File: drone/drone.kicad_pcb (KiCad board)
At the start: 2 copper layers, 53.3 x 55.2 mm, 52 parts, among them U1 ESP32-WROOM-32D, U2 MPU-6050, U3 MP2303ADN

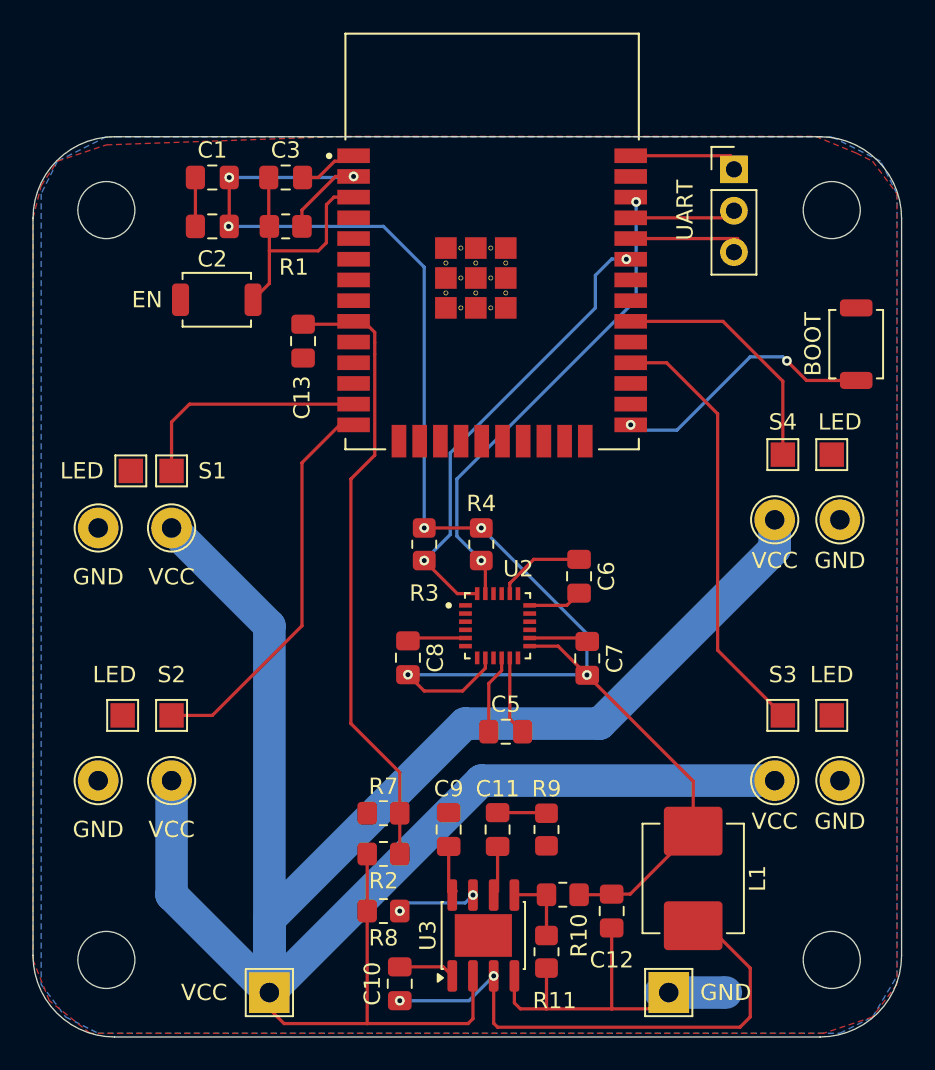
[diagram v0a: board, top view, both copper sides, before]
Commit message: tang width 3v3 len 0.4mm
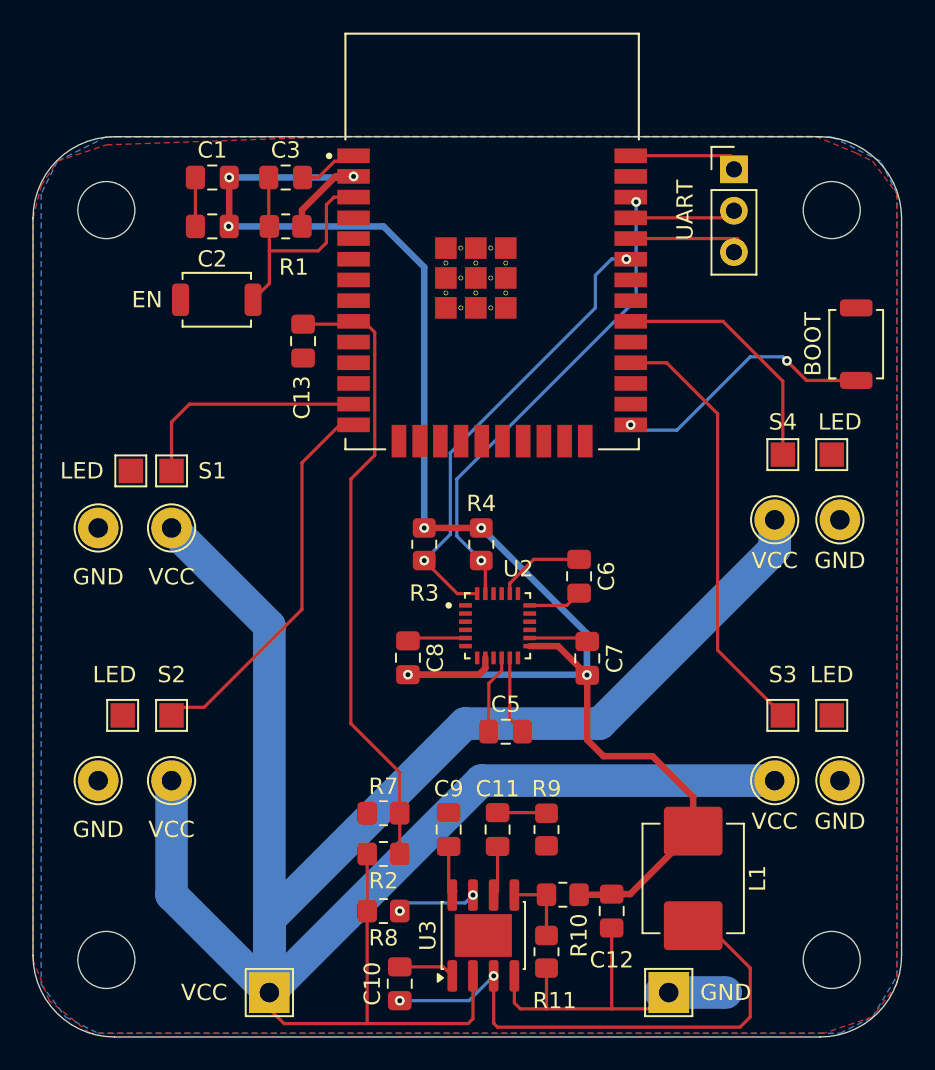
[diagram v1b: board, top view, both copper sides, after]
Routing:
- net +3V3: track 103.0 -> 103.9 mm
- net ESC2: track 24.4 -> 23.8 mm
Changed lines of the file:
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@@
 		(capping no)
 		(filling no)
+		(zone_defaults)
 		(pcbplotparams
 			(layerselection 0x00000000_00000000_55555555_5755f5ff)
@@
 	)
 	(segment
-		(start 203.5 74.5)
-		(end 205.565 72.435)
-		(width 0.2)
+		(start 219.2125 101.25)
+		(end 217.47 101.25)
+		(width 0.4)
 		(layer "F.Cu")
 		(net "+3V3")
 	)
 	(segment
-		(start 219.2125 101.25)
-		(end 220.98125 103.01875)
-		(width 0.2)
+		(start 210 103)
+		(end 214.355 103)
+		(width 0.4)
 		(layer "F.Cu")
 		(net "+3V3")
 	)
 	(segment
-		(start 203.5 75.5)
-		(end 203.5 74.5)
-		(width 0.2)
+		(start 225 108)
+		(end 222 108)
+		(width 0.4)
 		(layer "F.Cu")
 		(net "+3V3")
 	)
 	(segment
-		(start 227.5 109.5375)
-		(end 227.5 112.6)
-		(width 0.2)
+		(start 227.5 110.5)
+		(end 225 108)
+		(width 0.4)
 		(layer "F.Cu")
 		(net "+3V3")
 	)
 	(segment
-		(start 199.0375 72.5)
-		(end 199.0375 76)
-		(width 0.2)
+		(start 203.5 74.5)
+		(end 205.565 72.435)
+		(width 0.4)
 		(layer "F.Cu")
 		(net "+3V3")
 	)
 	(segment
-		(start 213.355 104)
-		(end 211 104)
-		(width 0.2)
+		(start 214.355 103)
+		(end 214.75 102.605)
+		(width 0.4)
 		(layer "F.Cu")
 		(net "+3V3")
 	)
 	(segment
-		(start 214.75 102.605)
-		(end 213.355 104)
-		(width 0.2)
+		(start 203.5 75.5)
+		(end 203.5 74.5)
+		(width 0.4)
 		(layer "F.Cu")
 		(net "+3V3")
 	)
 	(segment
-		(start 220.98125 103.01875)
-		(end 221 103.0375)
-		(width 0.2)
+		(start 199.0375 72.5)
+		(end 199.0375 76)
+		(width 0.4)
 		(layer "F.Cu")
 		(net "+3V3")
 	)
 	(segment
-		(start 205.565 72.435)
-		(end 206.665 72.435)
-		(width 0.2)
+		(start 214.75 102.605)
+		(end 214.75 101.97)
+		(width 0.4)
 		(layer "F.Cu")
 		(net "+3V3")
 	)
 	(segment
-		(start 214.75 101.97)
-		(end 214.75 102.605)
-		(width 0.2)
+		(start 223.6375 116.4625)
+		(end 227.5 112.6)
+		(width 0.4)
 		(layer "F.Cu")
 		(net "+3V3")
 	)
 	(segment
-		(start 222.5 116.4625)
+		(start 220.5 116.5)
 		(end 222.4625 116.5)
-		(width 0.2)
+		(width 0.4)
 		(layer "F.Cu")
 		(net "+3V3")
 	)
 	(segment
-		(start 227.5 109.5375)
+		(start 221 107)
 		(end 221 103.0375)
-		(width 0.2)
+		(width 0.4)
 		(layer "F.Cu")
 		(net "+3V3")
 	)
 	(segment
-		(start 223.6375 116.4625)
-		(end 227.5 112.6)
-		(width 0.2)
+		(start 220.98125 103.01875)
+		(end 221 103.0375)
+		(width 0.4)
+		(layer "F.Cu")
+		(net "+3V3")
+	)
+	(segment
+		(start 205.565 72.435)
+		(end 206.665 72.435)
+		(width 0.4)
 		(layer "F.Cu")
 		(net "+3V3")
@@
 	(segment
 		(start 222.4625 116.5)
-		(end 220.5 116.5)
-		(width 0.2)
+		(end 222.5 116.4625)
+		(width 0.4)
+		(layer "F.Cu")
+		(net "+3V3")
+	)
+	(segment
+		(start 222 108)
+		(end 221 107)
+		(width 0.4)
 		(layer "F.Cu")
 		(net "+3V3")
 	)
 	(segment
-		(start 217.47 101.25)
+		(start 220.98125 103.01875)
 		(end 219.2125 101.25)
-		(width 0.2)
+		(width 0.4)
 		(layer "F.Cu")
 		(net "+3V3")
@@
 		(start 211 94)
 		(end 214.5 94)
-		(width 0.2)
+		(width 0.4)
 		(layer "F.Cu")
 		(net "+3V3")
@@
 		(start 222.5 116.4625)
 		(end 223.6375 116.4625)
-		(width 0.2)
+		(width 0.4)
 		(layer "F.Cu")
 		(net "+3V3")
 	)
 	(segment
-		(start 211 104)
-		(end 210 103)
-		(width 0.2)
+		(start 227.5 112.6)
+		(end 227.5 110.5)
+		(width 0.4)
 		(layer "F.Cu")
 		(net "+3V3")
@@
 		(start 199 75.5)
 		(end 199.0375 75.5)
-		(width 0.2)
+		(width 0.4)
 		(layer "B.Cu")
 		(net "+3V3")
@@
 		(start 211 94)
 		(end 211 78)
-		(width 0.2)
+		(width 0.4)
 		(layer "B.Cu")
 		(net "+3V3")
@@
 		(start 206.6 72.5)
 		(end 199.0375 72.5)
-		(width 0.2)
+		(width 0.4)
 		(layer "B.Cu")
 		(net "+3V3")
@@
 		(start 220.9625 103)
 		(end 210 103)
-		(width 0.2)
-		(layer "B.Cu")
-		(net "+3V3")
-	)
-	(segment
-		(start 220.98125 103.01875)
-		(end 220.9625 103)
-		(width 0.2)
+		(width 0.4)
 		(layer "B.Cu")
 		(net "+3V3")
@@
 		(start 220.98125 100.48125)
 		(end 220.98125 103.01875)
-		(width 0.2)
+		(width 0.4)
 		(layer "B.Cu")
 		(net "+3V3")
@@
 		(start 211 78)
 		(end 208.5 75.5)
-		(width 0.2)
+		(width 0.4)
 		(layer "B.Cu")
 		(net "+3V3")
@@
 		(start 208.5 75.5)
 		(end 199 75.5)
-		(width 0.2)
+		(width 0.4)
 		(layer "B.Cu")
 		(net "+3V3")
@@
 		(start 206.665 72.435)
 		(end 206.6 72.5)
-		(width 0.2)
+		(width 0.4)
+		(layer "B.Cu")
+		(net "+3V3")
+	)
+	(segment
+		(start 220.98125 103.01875)
+		(end 220.9625 103)
+		(width 0.4)
 		(layer "B.Cu")
 		(net "+3V3")
@@
 		(start 214.5 94)
 		(end 220.98125 100.48125)
-		(width 0.2)
+		(width 0.4)
 		(layer "B.Cu")
 		(net "+3V3")
@@
 	)
 	(segment
-		(start 205.825 87.675)
-		(end 206.665 87.675)
+		(start 203.5 99)
+		(end 203.5 90)
 		(width 0.2)
 		(layer "F.Cu")
@@
 	)
 	(segment
-		(start 195.5 105.5)
-		(end 198 105.5)
+		(start 196 105)
+		(end 197.5 105)
 		(width 0.2)
 		(layer "F.Cu")
@@
 	)
 	(segment
-		(start 203.5 100)
-		(end 203.5 90)
+		(start 205.825 87.675)
+		(end 206.665 87.675)
 		(width 0.2)
 		(layer "F.Cu")
@@
 	)
 	(segment
-		(start 198 105.5)
-		(end 203.5 100)
+		(start 195.5 105.5)
+		(end 196 105)
+		(width 0.2)
+		(layer "F.Cu")
+		(net "ESC2")
+	)
+	(segment
+		(start 197.5 105)
+		(end 203.5 99)
 		(width 0.2)
 		(layer "F.Cu")

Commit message: led with gnd
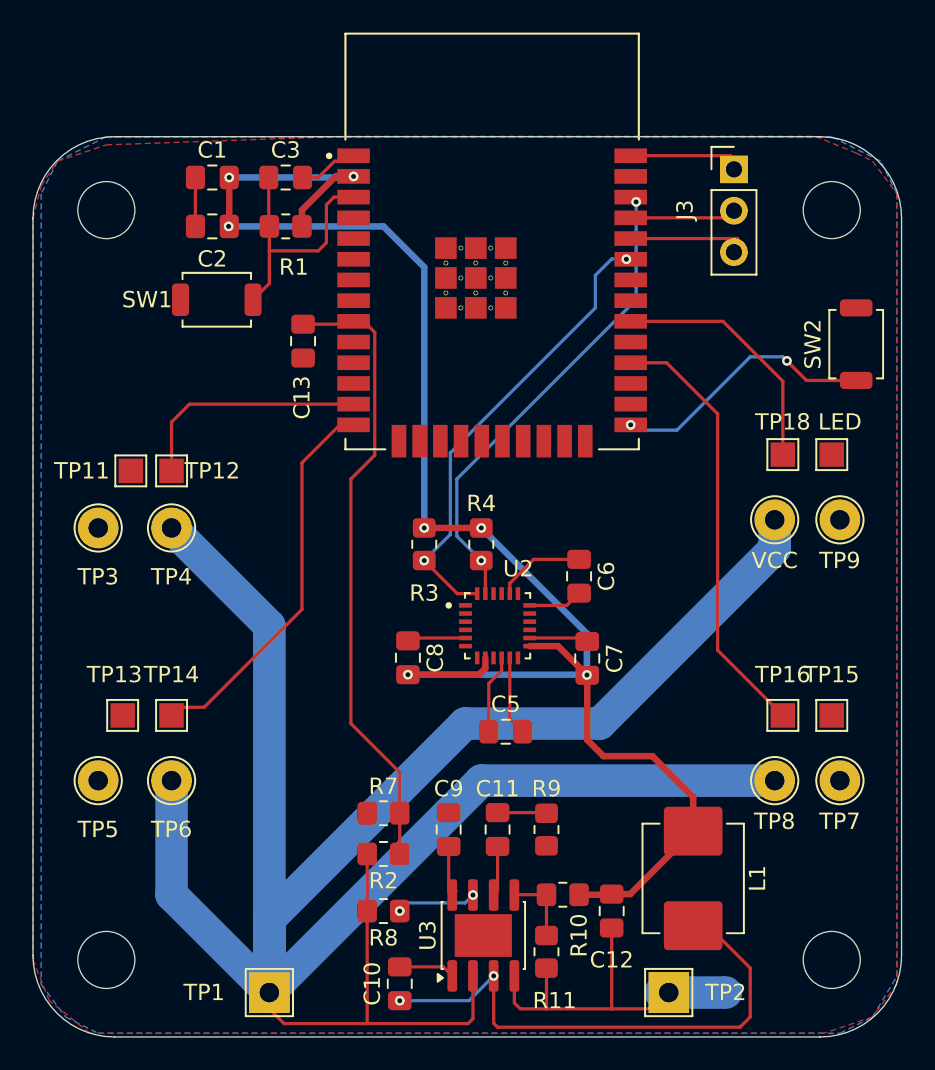
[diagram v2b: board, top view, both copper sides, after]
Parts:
- renumbered UART to J3, EN to SW1, BOOT to SW2, VCC to TP1, LED to TP11, S1 to TP12, LED to TP13, S2 to TP14, LED to TP15, S3 to TP16, S4 to TP18, GND to TP2, GND to TP3, VCC to TP4, GND to TP5, VCC to TP6, GND to TP7, VCC to TP8, GND to TP9
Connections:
- TP11 pad 1: unconnected-(TP11-Pad1) -> GND
- TP13 pad 1: unconnected-(TP13-Pad1) -> GND
- TP15 pad 1: unconnected-(TP15-Pad1) -> GND
- TP17 pad 1: unconnected-(TP17-Pad1) -> GND
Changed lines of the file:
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@@
 		(capping no)
 		(filling no)
-		(zone_defaults)
 		(pcbplotparams
 			(layerselection 0x00000000_00000000_55555555_5755f5ff)
@@
 		(descr "SMD pad as test Point, diameter 2.5mm")
 		(tags "test point SMD pad")
-		(property "Reference" "GND"
+		(property "Reference" "TP7"
 			(at 0 2.5 0)
 			(layer "F.SilkS")
@@
 		(descr "SMD pad as test Point, diameter 2.5mm")
 		(tags "test point SMD pad")
-		(property "Reference" "VCC"
+		(property "Reference" "TP6"
 			(at 0 3 180)
 			(layer "F.SilkS")
@@
 		(descr "SMD rectangular pad as test Point, square 1.5mm side length")
 		(tags "test point SMD pad rectangle square")
-		(property "Reference" "S2"
+		(property "Reference" "TP14"
 			(at 0 2.5 180)
 			(layer "F.SilkS")
@@
 		(descr "SMD rectangular pad as test Point, square 2.5mm side length")
 		(tags "test point SMD pad rectangle square")
-		(property "Reference" "GND"
+		(property "Reference" "TP2"
 			(at 3.5 0 0)
 			(layer "F.SilkS")
@@
 		(descr "SMD rectangular pad as test Point, square 1.5mm side length")
 		(tags "test point SMD pad rectangle square")
-		(property "Reference" "S3"
+		(property "Reference" "TP16"
 			(at 0 -2.5 0)
 			(layer "F.SilkS")
@@
 		(descr "SMD rectangular pad as test Point, square 1.5mm side length")
 		(tags "test point SMD pad rectangle square")
-		(property "Reference" "S1"
+		(property "Reference" "TP12"
 			(at 0 -2.5 0)
 			(layer "F.SilkS")
@@
 		(descr "SMD rectangular pad as test Point, square 1.5mm side length")
 		(tags "test point SMD pad rectangle square")
-		(property "Reference" "S4"
+		(property "Reference" "TP18"
 			(at 0 -2 180)
 			(layer "F.SilkS")
@@
 			(size 1.5 1.5)
 			(layers "F.Cu" "F.Mask")
-			(net "unconnected-(TP17-Pad1)")
+			(net "GND")
 			(pinfunction "1_1")
-			(pintype "passive+no_connect")
+			(pintype "passive")
 		)
 		(embedded_fonts no)
@@
 		(descr "SMD pad as test Point, diameter 2.5mm")
 		(tags "test point SMD pad")
-		(property "Reference" "GND"
+		(property "Reference" "TP5"
 			(at 0 3 180)
 			(layer "F.SilkS")
@@
 		(descr "SMD pad as test Point, diameter 2.5mm")
 		(tags "test point SMD pad")
-		(property "Reference" "VCC"
+		(property "Reference" "TP8"
 			(at 0 2.5 0)
 			(layer "F.SilkS")
@@
 		(descr "SMD pad as test Point, diameter 2.5mm")
 		(tags "test point SMD pad")
-		(property "Reference" "GND"
+		(property "Reference" "TP3"
 			(at 0 3 180)
 			(layer "F.SilkS")
@@
 		(descr "SMD rectangular pad as test Point, square 1.5mm side length")
 		(tags "test point SMD pad rectangle square")
-		(property "Reference" "LED"
+		(property "Reference" "TP11"
 			(at 0 3 0)
 			(layer "F.SilkS")
@@
 			(size 1.5 1.5)
 			(layers "F.Cu" "F.Mask")
-			(net "unconnected-(TP11-Pad1)")
+			(net "GND")
 			(pinfunction "1_1")
-			(pintype "passive+no_connect")
+			(pintype "passive")
 		)
 		(embedded_fonts no)
@@
 		(descr "SMD rectangular pad as test Point, square 1.5mm side length")
 		(tags "test point SMD pad rectangle square")
-		(property "Reference" "LED"
+		(property "Reference" "TP13"
 			(at -2.5 0.5 180)
 			(layer "F.SilkS")
@@
 			(size 1.5 1.5)
 			(layers "F.Cu" "F.Mask")
-			(net "unconnected-(TP13-Pad1)")
+			(net "GND")
 			(pinfunction "1_1")
-			(pintype "passive+no_connect")
+			(pintype "passive")
 		)
 		(embedded_fonts no)
@@
 		(descr "SMD pad as test Point, diameter 2.5mm")
 		(tags "test point SMD pad")
-		(property "Reference" "VCC"
+		(property "Reference" "TP4"
 			(at 0 -3 180)
 			(layer "F.SilkS")
@@
 		(descr "SMD Tactile Switch, 3.9x3x2.5 mm, https://lcsc.com/datasheet/lcsc_datasheet_2504101957_XUNPU-TS-1088-AR02016_C720477.pdf")
 		(tags "Tactile Switch")
-		(property "Reference" "EN"
+		(property "Reference" "SW1"
 			(at -4.275 0 0)
 			(layer "F.SilkS")
@@
 		(descr "SMD rectangular pad as test Point, square 1.5mm side length")
 		(tags "test point SMD pad rectangle square")
-		(property "Reference" "LED"
+		(property "Reference" "TP15"
 			(at 0 -2.5 0)
 			(layer "F.SilkS")
@@
 			(size 1.5 1.5)
 			(layers "F.Cu" "F.Mask")
-			(net "unconnected-(TP15-Pad1)")
+			(net "GND")
 			(pinfunction "1_1")
-			(pintype "passive+no_connect")
+			(pintype "passive")
 		)
 		(embedded_fonts no)
@@
 		(descr "SMD Tactile Switch, 3.9x3x2.5 mm, https://lcsc.com/datasheet/lcsc_datasheet_2504101957_XUNPU-TS-1088-AR02016_C720477.pdf")
 		(tags "Tactile Switch")
-		(property "Reference" "BOOT"
+		(property "Reference" "SW2"
 			(at 0 -2.65 90)
 			(layer "F.SilkS")
@@
 		(descr "SMD rectangular pad as test Point, square 2.5mm side length")
 		(tags "test point SMD pad rectangle square")
-		(property "Reference" "VCC"
+		(property "Reference" "TP1"
 			(at -4 0 0)
 			(layer "F.SilkS")
@@
 		(descr "SMD pad as test Point, diameter 2.5mm")
 		(tags "test point SMD pad")
-		(property "Reference" "GND"
+		(property "Reference" "TP9"
 			(at 0 2.5 180)
 			(layer "F.SilkS")
@@
 		(descr "Through hole straight pin header, 1x03, 2.54mm pitch, single row")
 		(tags "Through hole pin header THT 1x03 2.54mm single row")
-		(property "Reference" "UART"
+		(property "Reference" "J3"
 			(at -3 2.5 90)
 			(layer "F.SilkS")

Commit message: hi
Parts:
- removed C5, C6: 220pF, Capacitor_SMD:C_0805_2012Metric_Pad1.18x1.45mm_HandSolder
- removed C7, C8: 0.1uF, Capacitor_SMD:C_0805_2012Metric_Pad1.18x1.45mm_HandSolder
- removed R3, R4: 4.7k, Resistor_SMD:R_0805_2012Metric_Pad1.20x1.40mm_HandSolder
- removed U2: MPU-6050, MPU-6050:QFN50P400X400X95-24N
- added C4: 10nF, Capacitor_SMD:C_0805_2012Metric_Pad1.18x1.45mm_HandSolder, F.Cu at (223.0, 94.5)
- added J1: Conn_01x04_Pin, Connector_PinSocket_2.54mm:PinSocket_1x04_P2.54mm_Vertical, F.Cu at (220.0, 94.0)
- H1, H2, H3, H4: footprint MountingHole:MountingHole_3.5mm -> MountingHole:MountingHole_3.2mm_M3
- TP10, TP3, TP4, TP5, TP6, TP7, TP8, TP9: footprint TestPoint:TestPoint_Pad_D2.5mm -> TestPoint:TestPoint_Pad_2.5x2.5mm; moved to B.Cu
- moved TP3 6.00 mm to (191.0, 88.0), turned to 180 degrees
- moved TP14 5.70 mm to (191.0, 109.0)
- moved TP9 5.52 mm to (236.0, 88.0), turned to 180 degrees
- moved TP4 5.15 mm to (191.0, 91.5), turned to 0 degrees
- moved TP12 4.61 mm to (191.0, 91.5)
- moved TP16 4.61 mm to (236.0, 109.0)
- moved TP6 4.53 mm to (191.0, 109.0), turned to 180 degrees
- moved TP10 4.03 mm to (236.0, 91.5), turned to 180 degrees
- moved TP7 4.03 mm to (236.0, 105.5), turned to 180 degrees
- moved TP5 4.00 mm to (191.0, 105.5), turned to 180 degrees
- moved C10 3.92 mm to (208.8, 118.1)
- moved C11 3.92 mm to (214.8, 108.7)
- moved C12 3.92 mm to (221.8, 113.7)
- moved C9 3.92 mm to (211.8, 108.7)
- moved NT1 3.92 mm to (226.8, 118.7)
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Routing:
- net GND: track 47.7 -> 30.7 mm
- net +3V3: track 103.9 -> 87.7 mm, vias 7 -> 4
- net ESC2: track 23.8 -> 32.1 mm
- net ESC VCC: track 156.1 -> 163.4 mm
- net SDA: track 28.3 -> 21.2 mm, vias 2 -> 1
- net ESC3: track 26.8 -> 33.9 mm
- net SCL: track 29.3 -> 34.9 mm, vias 2 -> 1
- net Net-(U2-CPOUT): track 5.49 -> 0.00 mm
- net Net-(U2-REGOUT): track 4.86 -> 0.00 mm
- net ESC4: track 15.4 -> 19.7 mm
- net Batt Read: track 39.1 -> 35.6 mm
- net ESC1: track 14.6 -> 17.8 mm
- net RX: track 7.70 -> 4.89 mm
- net TX: track 6.52 -> 4.36 mm
- net Net-(U1-IO0): track 16.9 -> 15.2 mm
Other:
- board size 53.3 x 55.2 mm -> 52 x 52 mm
